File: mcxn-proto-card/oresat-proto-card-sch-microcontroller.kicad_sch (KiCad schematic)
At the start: 25 parts, among them J7 ORESAT-DEBUG-CONNECTOR-ALL, U1 TCAN330, U7 STM32F091C, X2 CRYSTAL-WITH-GND

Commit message: Removed and replaced eagle libraries for C, R, and Power symbols
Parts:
- C13, C14, C15, C18, C19, C20, C21: symbol oresat-proto-card-eagle-import:C-EU0603-C-NOSILK -> Device:C_Small_US
- D5: symbol oresat-proto-card-eagle-import:LED-GREEN0603 -> Device:D_Small_Filled
- JP11, JP8: symbol oresat-proto-card-eagle-import:PINHD-2X10 -> Connector_Generic:Conn_02x10_Odd_Even
- R47, R48, R49, R50, R51: symbol oresat-proto-card-eagle-import:R-US_0603-C-NOSILK -> oresat-passives:R-US
- TP25, TP26, TP27, TP28, TP29, TP30: value TEST-POINT-LARGE-SQUARE -> Test-Point; footprint oresat-proto-card:1X01 -> oresat-misc:TestPoint-0.75mm-th; symbol oresat-proto-card-eagle-import:TEST-POINT-LARGE-SQUARE -> oresat-misc:Test-Point-0.75mm-th; now left out of the parts list
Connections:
- net GND: now also D5.1 (K); no longer D5.C
- net at R48.1: now also D5.2 (A); no longer D5.A

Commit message: Eagle libraries removed and replaced, schematic and layout clean up
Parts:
- C13, C14, C15, C18, C19, C20, C21: symbol Device:C_Small_US -> Device:C_Small
- D5: footprint oresat-proto-card:LED-0603 -> LED_SMD:LED_0603_1608Metric; symbol Device:D_Small_Filled -> Device:LED_Small_Filled
- J7: footprint oresat-proto-card:TE_2-1734592-0 -> oresat-connectors:J-TE-2-1734592-0; symbol oresat-proto-card-eagle-import:ORESAT-DEBUG-CONNECTOR-ALL -> oresat-connectors:oresat-debug-all
- JP11, JP8: footprint oresat-proto-card:2X10 -> Connector_PinHeader_2.54mm:PinHeader_2x10_P2.54mm_Vertical
- U1: footprint oresat-proto-card:SOT23-8_TI-DCN -> oresat-ics:SOT23-8_TI-DCN; symbol oresat-proto-card-eagle-import:TCAN330 -> oresat-ics:TCAN330; Distributor (none) -> DigiKey; MPN TCAN330GDCNT -> TCAN330GDCN
- X2: footprint oresat-proto-card:CRYSTAL_2.5X2 -> Crystal:Crystal_SMD_2520-4Pin_2.5x2.0mm; symbol oresat-proto-card-eagle-import:CRYSTAL-WITH-GND -> Device:Crystal_GND2_Small
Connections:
- net GND: no longer X2.4 (SHIELD)
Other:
- note added: "NOT YELLOW!! (Also, on PCB there is a courtyard issue with new footprint, but I don't want to move it case it connects to backplane or something)"
- note added: "it is labeled: STM32F091C HOWEVER the MPN is labeled: STM32F042K6T Which one is it????"
- note added: "written on this page BUT applies to 2nd page as well. (except for that weird 10k thingy)"

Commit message: Eagle libraries replaced, scheatic and layout clean up cont.
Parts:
- removed U1: TCAN330, oresat-ics:SOT23-8_TI-DCN, symbol oresat-ics:TCAN330
- added U4: TCAN330, Package_TO_SOT_SMD:SOT-23-8, symbol Interface_CAN_LIN:TCAN330
- J7: footprint oresat-connectors:J-TE-2-1734592-0 -> oresat-proto-card:TE_2-1734592-0; symbol oresat-connectors:oresat-debug-all -> oresat-connectors:ORESAT-DEBUG-CONNECTOR-ALL
- R50, R51: now not fitted
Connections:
- net 3.3V: now also U4.3 (VCC)
- net CAN2_H: now also U4.7 (CANH)
- net CAN2_L: now also U4.6 (CANL)
- net CAN_RX: now also U4.4 (RXD)
- net CAN_SHDN: now also U4.5 (SHDN)
- net CAN_TX: now also U4.1 (TXD)
- net GND: now also U4.2 (GND)
- net PA9/CAN_SILENT: now also U4.8 (S)
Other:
- note removed: "Emergency M0 bootstrapping over OPD I2C Address: 0b0111110x"
- note removed: "NOT YELLOW!! (Also, on PCB there is a courtyard issue with new footprint, but I don't want to move it case it connects to backplane or something)"

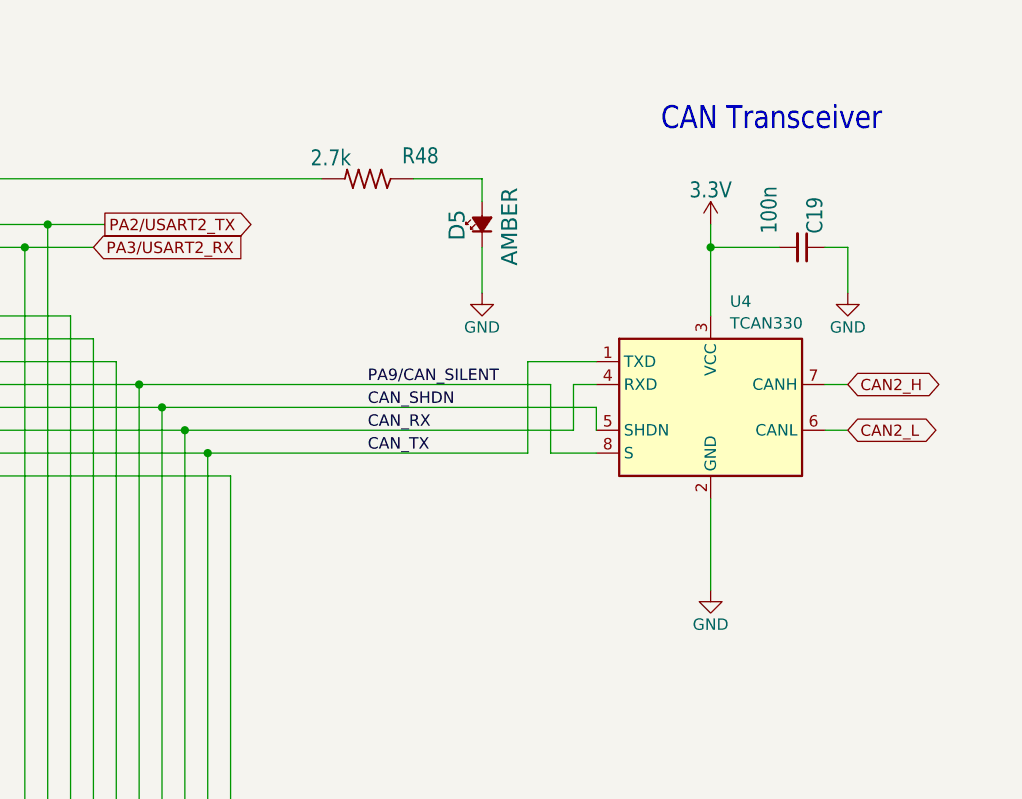
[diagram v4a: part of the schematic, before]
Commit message: Cleaned up layout and routing
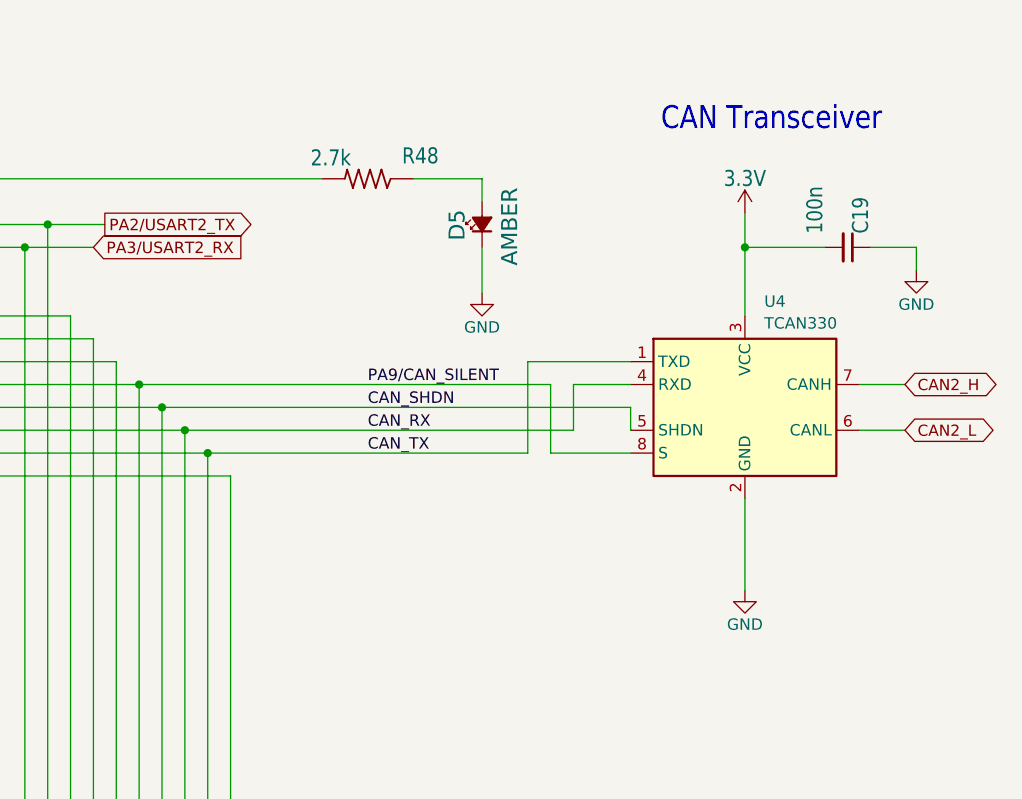
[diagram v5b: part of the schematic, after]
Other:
- moved on the sheet: C19, U4
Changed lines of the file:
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@@
 	)
 	(junction
-		(at 383.54 87.63)
-		(diameter 0)
-		(color 0 0 0 0)
-	)
-	(junction
 		(at 68.58 74.93)
 		(diameter 0)
@@
 	)
 	(junction
+		(at 387.35 87.63)
+		(diameter 0)
+		(color 0 0 0 0)
+	)
+	(junction
 		(at 220.98 21.59)
 		(diameter 0)
@@
 	(wire
 		(pts
-			(xy 383.54 87.63) (xy 391.16 87.63)
-		)
-		(stroke
-			(width 0.1524)
-			(type solid)
-		)
-	)
-	(wire
-		(pts
 			(xy 116.84 229.87) (xy 142.24 229.87)
 		)
@@
 	(wire
 		(pts
-			(xy 398.78 87.63) (xy 398.78 92.71)
+			(xy 406.4 87.63) (xy 406.4 90.17)
 		)
 		(stroke
@@
 	(wire
 		(pts
-			(xy 383.54 87.63) (xy 383.54 95.25)
+			(xy 387.35 87.63) (xy 387.35 95.25)
 		)
 		(stroke
@@
 	(wire
 		(pts
+			(xy 387.35 115.57) (xy 387.35 125.73)
+		)
+		(stroke
+			(width 0.1524)
+			(type solid)
+		)
+	)
+	(wire
+		(pts
 			(xy 43.18 57.15) (xy 33.02 57.15)
 		)
@@
 	(wire
 		(pts
-			(xy 322.58 105.41) (xy 370.84 105.41)
+			(xy 322.58 105.41) (xy 374.65 105.41)
 		)
 		(stroke
@@
 	(wire
 		(pts
-			(xy 396.24 87.63) (xy 398.78 87.63)
+			(xy 401.32 87.63) (xy 406.4 87.63)
 		)
 		(stroke
@@
 	(wire
 		(pts
-			(xy 383.54 87.63) (xy 383.54 85.09)
+			(xy 387.35 87.63) (xy 387.35 83.82)
 		)
 		(stroke
@@
 	(wire
 		(pts
-			(xy 365.76 110.49) (xy 370.84 110.49)
+			(xy 365.76 110.49) (xy 374.65 110.49)
 		)
 		(stroke
@@
 	(wire
 		(pts
-			(xy 383.54 115.57) (xy 383.54 125.73)
-		)
-		(stroke
-			(width 0.1524)
-			(type solid)
-		)
-	)
-	(wire
-		(pts
 			(xy 271.78 163.83) (xy 271.78 90.17)
 		)
@@
 	(wire
 		(pts
-			(xy 370.84 100.33) (xy 363.22 100.33)
+			(xy 374.65 100.33) (xy 363.22 100.33)
 		)
 		(stroke
@@
 	(wire
 		(pts
-			(xy 396.24 102.87) (xy 398.78 102.87)
+			(xy 400.05 102.87) (xy 405.13 102.87)
 		)
 		(stroke
@@
 	(wire
 		(pts
-			(xy 396.24 107.95) (xy 398.78 107.95)
+			(xy 400.05 107.95) (xy 405.13 107.95)
 		)
 		(stroke
@@
 	(wire
 		(pts
-			(xy 370.84 102.87) (xy 368.3 102.87)
+			(xy 374.65 102.87) (xy 368.3 102.87)
 		)
 		(stroke
@@
 	(wire
 		(pts
+			(xy 387.35 87.63) (xy 396.24 87.63)
+		)
+		(stroke
+			(width 0.1524)
+			(type solid)
+		)
+	)
+	(wire
+		(pts
 			(xy 246.38 82.55) (xy 279.4 82.55)
 		)
@@
 	(wire
 		(pts
-			(xy 370.84 105.41) (xy 370.84 107.95)
+			(xy 374.65 105.41) (xy 374.65 107.95)
 		)
 		(stroke
@@
 	(global_label "CAN2_L"
 		(shape bidirectional)
-		(at 398.78 107.95 0)
+		(at 405.13 107.95 0)
 		(fields_autoplaced yes)
 		(effects
@@
 		)
 		(property "Intersheetrefs" "${INTERSHEET_REFS}"
-			(at 409.5506 107.95 0)
+			(at 415.9006 107.95 0)
 			(effects
 				(font
@@
 	(global_label "CAN2_H"
 		(shape bidirectional)
-		(at 398.78 102.87 0)
+		(at 405.13 102.87 0)
 		(fields_autoplaced yes)
 		(effects
@@
 		)
 		(property "Intersheetrefs" "${INTERSHEET_REFS}"
-			(at 409.847 102.87 0)
+			(at 416.197 102.87 0)
 			(effects
 				(font
@@
 	(symbol
 		(lib_id "Device:C_Small")
-		(at 393.7 87.63 270)
+		(at 398.78 87.63 270)
 		(mirror x)
 		(unit 1)
@@
 		(dnp no)
 		(property "Reference" "C19"
-			(at 394.081 86.106 0)
+			(at 399.161 86.106 0)
 			(effects
 				(font
@@
 		)
 		(property "Value" "100n"
-			(at 389.001 86.106 0)
+			(at 394.081 86.106 0)
 			(effects
 				(font
@@
 		)
 		(property "Footprint" "oresat-passives:0603-C-NOSILK"
-			(at 393.7 87.63 0)
+			(at 398.78 87.63 0)
 			(effects
 				(font
@@
 		)
 		(property "Datasheet" "~"
-			(at 393.7 87.63 0)
+			(at 398.78 87.63 0)
 			(effects
 				(font
@@
 		)
 		(property "Description" "Unpolarized capacitor, small symbol"
-			(at 393.7 87.63 0)
+			(at 398.78 87.63 0)
 			(effects
 				(font
@@
 		)
 		(property "DIS" "Digi-Key"
-			(at 393.7 87.63 0)
+			(at 398.78 87.63 0)
 			(effects
 				(font
@@
 		)
 		(property "DPN" "1276-1001-1-ND"
-			(at 393.7 87.63 0)
+			(at 398.78 87.63 0)
 			(effects
 				(font
@@
 		)
 		(property "MFR" "Samsung"
-			(at 393.7 87.63 0)
+			(at 398.78 87.63 0)
 			(effects
 				(font
@@
 		)
 		(property "MPN" "CL05B104KO5NNNC"
-			(at 393.7 87.63 0)
+			(at 398.78 87.63 0)
 			(effects
 				(font
@@
 	(symbol
 		(lib_id "power:GND")
-		(at 383.54 125.73 0)
+		(at 387.35 125.73 0)
 		(mirror y)
 		(unit 1)
@@
 		(dnp no)
 		(property "Reference" "#GND057"
-			(at 383.54 125.73 0)
+			(at 387.35 125.73 0)
 			(effects
 				(font
@@
 		)
 		(property "Value" "GND"
-			(at 383.54 129.54 0)
+			(at 387.35 129.54 0)
 			(effects
 				(font
@@
 		)
 		(property "Footprint" ""
-			(at 383.54 125.73 0)
+			(at 387.35 125.73 0)
 			(effects
 				(font
@@
 		)
 		(property "Datasheet" ""
-			(at 383.54 125.73 0)
+			(at 387.35 125.73 0)
 			(effects
 				(font
@@
 		)
 		(property "Description" "Power symbol creates a global label with name \"GND\" , ground"
-			(at 383.54 125.73 0)
+			(at 387.35 125.73 0)
 			(effects
 				(font
@@
 	(symbol
 		(lib_id "power:+3.3V")
-		(at 383.54 85.09 0)
+		(at 387.35 83.82 0)
 		(mirror y)
 		(unit 1)
@@
 		(dnp no)
 		(property "Reference" "#SUPPLY09"
-			(at 383.54 85.09 0)
+			(at 387.35 83.82 0)
 			(effects
 				(font
@@
 		)
 		(property "Value" "3.3V"
-			(at 383.54 82.296 0)
+			(at 387.35 81.026 0)
 			(effects
 				(font
@@
 		)
 		(property "Footprint" ""
-			(at 383.54 85.09 0)
+			(at 387.35 83.82 0)
 			(effects
 				(font
@@
 		)
 		(property "Datasheet" ""
-			(at 383.54 85.09 0)
+			(at 387.35 83.82 0)
 			(effects
 				(font
@@
 		)
 		(property "Description" "Power symbol creates a global label with name \"+3.3V\""
-			(at 383.54 85.09 0)
+			(at 387.35 83.82 0)
 			(effects
 				(font
@@
 	(symbol
 		(lib_id "Interface_CAN_LIN:TCAN330")
-		(at 383.54 105.41 0)
+		(at 387.35 105.41 0)
 		(unit 1)
 		(exclude_from_sim no)
@@
 		(fields_autoplaced yes)
 		(property "Reference" "U4"
-			(at 385.6833 93.6455 0)
+			(at 389.4933 93.6455 0)
 			(effects
 				(font
@@
 		)
 		(property "Value" "TCAN330"
-			(at 385.6833 96.0698 0)
+			(at 389.4933 96.0698 0)
 			(effects
 				(font
@@
 		)
 		(property "Footprint" "Package_TO_SOT_SMD:SOT-23-8"
-			(at 383.54 118.11 0)
+			(at 387.35 118.11 0)
 			(effects
 				(font
@@
 		)
 		(property "Datasheet" "http://www.ti.com/lit/ds/symlink/tcan337.pdf"
-			(at 383.54 105.41 0)
+			(at 387.35 105.41 0)
 			(effects
 				(font
@@
 		)
 		(property "Description" "High-Speed CAN Transceiver, 1Mbps, 3.3V supply, silent mode, shutdown mode, SOT-23-8/SOIC-8"
-			(at 383.54 105.41 0)
+			(at 387.35 105.41 0)
 			(effects
 				(font
@@
 	(symbol
 		(lib_id "power:GND")
-		(at 398.78 92.71 0)
+		(at 406.4 90.17 0)
 		(mirror y)
 		(unit 1)
@@
 		(dnp no)
 		(property "Reference" "#GND056"
-			(at 398.78 92.71 0)
+			(at 406.4 90.17 0)
 			(effects
 				(font
@@
 		)
 		(property "Value" "GND"
-			(at 398.78 96.52 0)
+			(at 406.4 93.98 0)
 			(effects
 				(font
@@
 		)
 		(property "Footprint" ""
-			(at 398.78 92.71 0)
+			(at 406.4 90.17 0)
 			(effects
 				(font
@@
 		)
 		(property "Datasheet" ""
-			(at 398.78 92.71 0)
+			(at 406.4 90.17 0)
 			(effects
 				(font
@@
 		)
 		(property "Description" "Power symbol creates a global label with name \"GND\" , ground"
-			(at 398.78 92.71 0)
+			(at 406.4 90.17 0)
 			(effects
 				(font

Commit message: Fixed linked library footprints and routing
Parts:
- J7: footprint oresat-proto-card:TE_2-1734592-0 -> oresat-connectors:J-TE-2-1734592-0
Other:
- note added: "Look at datasheet pg 30. Different layout guideline for filtering and etc (for 3MHz to 3GHz)"
- note removed: "it is labeled: STM32F091C HOWEVER the MPN is labeled: STM32F042K6T Which one is it????"
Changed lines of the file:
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@@
 		)
 	)
-	(text "it is labeled: STM32F091C\nHOWEVER the MPN is labeled: STM32F042K6T\nWhich one is it????"
+	(text "Look at datasheet pg 30. Different layout guideline for filtering and etc (for 3MHz to 3GHz)"
 		(exclude_from_sim no)
-		(at 231.14 128.524 0)
+		(at 379.984 118.11 0)
 		(effects
 			(font
 				(size 1.27 1.27)
 			)
-			(justify left)
 		)
 	)
@@
 				)
 				(justify left bottom)
-				(hide yes)
 			)
 		)
@@
 			)
 		)
-		(property "Footprint" "oresat-proto-card:TE_2-1734592-0"
+		(property "Footprint" "oresat-connectors:J-TE-2-1734592-0"
 			(at 26.67 191.77 0)
 			(effects

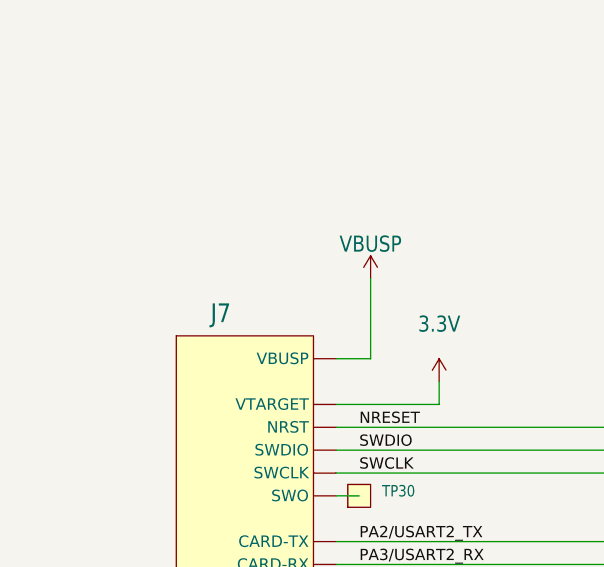
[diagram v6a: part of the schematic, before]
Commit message: Fixed schematic and routing for 2x11 connector
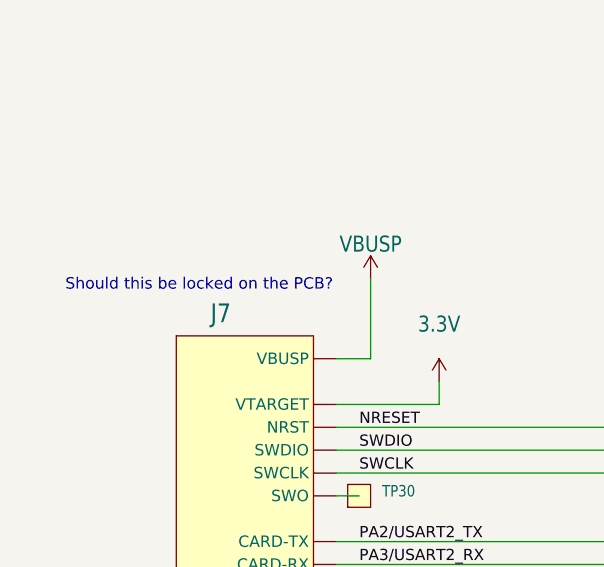
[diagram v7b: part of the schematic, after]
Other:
- note added: "Should this be locked on the PCB?"
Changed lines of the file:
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@@
+		)
+	)
+	(text "Should this be locked on the PCB?"
+		(exclude_from_sim no)
+		(at 22.86 155.702 0)
+		(effects
+			(font
+				(size 1.27 1.27)
+			)
 		)
 	)

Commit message: Fully routed MCXN947 proto card, still needs final polish.
Big cleanup of the proto card's OPD, bringing it up to modern standards. Also fixed the v2 backplane connector. Added the MCXN937 processor, and breakouts for the unused pins. Switched to the new debug connector, which will be fun. That's it!
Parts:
- removed C13, C14, C19, C20, C21: 100n, oresat-passives:0603-C-NOSILK, symbol Device:C_Small
- removed C15, C18: 20p, oresat-passives:0603-C-NOSILK, symbol Device:C_Small
- removed D5: AMBER, LED_SMD:LED_0603_1608Metric, symbol Device:LED_Small_Filled
- removed J7: ORESAT-DEBUG-CONNECTOR-ALL, oresat-connectors:J-TE-2-1734592-0, symbol oresat-connectors:ORESAT-DEBUG-CONNECTOR-ALL
- removed JP11, JP8: PINHD-2X10, Connector_PinHeader_2.54mm:PinHeader_2x10_P2.54mm_Vertical, symbol Connector_Generic:Conn_02x10_Odd_Even
- removed R47, R49: 10k, oresat-passives:0603-C-NOSILK, symbol oresat-passives:R-US
- removed R48: 2.7k, oresat-passives:0603-C-NOSILK, symbol oresat-passives:R-US
- removed R50, R51: 4.7k, oresat-passives:0603-C-NOSILK, symbol oresat-passives:R-US
- removed U4: TCAN330, Package_TO_SOT_SMD:SOT-23-8, symbol Interface_CAN_LIN:TCAN330
- removed U7: STM32F091C, oresat-proto-card:STM32F091C, symbol oresat-proto-card-eagle-import:STM32F091C
- removed X2: CRYSTAL-WITH-GND, Crystal:Crystal_SMD_2520-4Pin_2.5x2.0mm, symbol Device:Crystal_GND2_Small
- added C12, C24, C26, C28, C46, C48, C49, C50, C51, C52, C53, C7: 100n, oresat-passives:0603-C-NOSILK, symbol Device:C_Small
- added C25, C6: 4.7p, oresat-passives:0603-C-NOSILK, symbol Device:C_Small
- added C27, C30: 4.7u, oresat-passives:0603-C-NOSILK, symbol Device:C_Small
- added C29: 6.8u, oresat-passives:0603-C-NOSILK, symbol Device:C_Small
- added C31: 2.2u, oresat-passives:0603-C-NOSILK, symbol Device:C_Small
- added C47: 1u, oresat-passives:0603-C-NOSILK, symbol Device:C_Small
- added D4: AMBER, LED_SMD:LED_0603_1608Metric, symbol Device:LED_Small_Filled
- added FB1: 120 ohm, oresat-passives:0805-B-NOSILK, symbol Device:FerriteBead_Small
- added J9: SM14B-SHLS-TF, oresat-connectors:J-JST-SM14BSHLSTF, symbol oresat-connectors:ORESAT-DEBUG-CONNECTOR-3
- added L3: 1.5u, Inductor_SMD:L_0805_2012Metric, symbol Device:L_Small
- added R15: 10k, oresat-passives:0603-C-NOSILK, symbol Device:R_Small_US
- added R21: 1k, oresat-passives:0603-C-NOSILK, symbol Device:R_US
- added R23, R8: 4.7k, oresat-passives:0603-C-NOSILK, symbol Device:R_US
- added R9: 10k, oresat-passives:0603-C-NOSILK, symbol Device:R_US
- added TP10, TP11, TP12, TP13, TP14, TP16, TP17, TP18, TP19, TP20, TP22, TP3, TP32, TP33, TP41, TP42, TP43, TP44, TP45, TP46, TP47, TP48, TP49, TP5, TP50, TP51, TP52, TP53, TP54, TP55, TP56, TP57, TP58, TP59, TP6, TP60, TP61, TP62, TP63, TP64, TP65, TP66, TP67, TP68, TP69, TP7, TP70, TP71, TP72, TP73, TP74, TP75, TP76, TP77, TP78, TP79, TP8, TP80, TP81, TP82, TP83, TP84, TP85, TP86, TP9: Test-Point, oresat-misc:TestPoint-0.75mm-th, symbol oresat-misc:Test-Point-0.75mm-th
- added U1: MCXN947VKLT, oresat-ics:MCXN947KVLT-QFP50P1600X1600X160-101N, symbol oresat-ics:MCXN947VKLT
- added U8: TCAN330, Package_TO_SOT_SMD:SOT-23-8, symbol Interface_CAN_LIN:TCAN330
- added Y2: 24 MHz, Crystal:Crystal_SMD_2016-4Pin_2.0x1.6mm, symbol Device:Crystal_GND24_Small
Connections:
- net CAN2_H: now also U8.7 (CANH)
- net CAN2_L: now also U8.6 (CANL)
- net GND: now also C12.2, C24.2, C25.2, C26.2, C27.2, C28.2, C29.2, C30.2, C31.2, C46.2, C47.2, C48.2, C49.2, C50.2, C51.2, C52.2, C53.2, C6.2, C7.2, D4.1 (K), J9.14 (GND), J9.15 (PAD), J9.16 (PAD), J9.5 (GND), U1.101 (EP), U1.32 (VREFL), U1.33 (VSS_P4), U1.52 (VSS_DCDC), U8.2 (GND), Y2.2, Y2.4
- net SWCLK: now also J9.12 (SWCLK), U1.77 (P0_1)
- net SWDIO: now also J9.11 (SWDIO), U1.76 (P0_0)
- net VBUSP: now also J9.1 (VBUSP), J9.2 (VBUSP)
- net P4_2: now reaches TP28.1
- net P4_2: now also U1.24 (P4_2)
- net P4_0: now reaches TP30.1
- net P4_0: now also U1.22 (P4_0/ANA_0)
- net P4_4: now reaches TP26.1
- net P4_4: now also U1.26 (P4_4/ANA_4)
- net P4_3: now reaches TP27.1
- net P4_3: now also U1.25 (P4_3)
- net P4_1: now reaches TP29.1
- net P4_1: now also U1.23 (P4_1/ANA_1)
- net BOOT0 renamed P4_5
- net P4_5: now also U1.27 (P4_5/ANA_5)
- new net: C6.1, U1.11 (P1_31), Y2.1
- new net: U1.3 (P1_10), U8.1 (TXD)
- new net: U1.4 (P1_11), U8.4 (RXD)
- new net: C25.1, U1.10 (P1_30), Y2.3
- new net: D4.2 (A), R21.2
- new net: R21.1, U1.6 (P1_13)
- new net: J9.8 (DEBUG-0), TP6.1
- new net: L3.2, U1.53 (DCDC_LX)
- new net +3.3V: C24.1, C28.1, C30.1, C46.1, C48.1, C49.1, C50.1, C51.1, C52.1, C53.1, C7.1, FB1.1, J9.9 (VTARGET), R15.2, R23.2, R8.2, R9.2, U1.13 (VDD_LDO_CORE/VDD/VDD_P2), U1.34 (VDD_P4), U1.44 (VDD_USB), U1.47 (VDD_BAT), U1.54 (VDD_DCDC/VDD_LDO_SYS), U1.59 (VDD_P3), U1.66 (VDD_P3), U1.73 (VDD_P3), U1.83 (VDD), U1.96 (VDD), U8.3 (VCC)
- new net ISP-UART_RXD: J9.7 (CARD-RX), TP3.1, U1.1 (P1_8)
- new net ISP-UART_TXD: J9.6 (CARD-TX), TP13.1, U1.2 (P1_9)
- new net P0_18: TP78.1, U1.86 (P0_18)
- new net P0_19: TP79.1, U1.87 (P0_19)
- new net P0_20: TP80.1, U1.88 (P0_20)
- new net P0_21: TP81.1, U1.89 (P0_21)
- new net P0_22: TP82.1, U1.90 (P0_22)
- new net P0_23: TP83.1, U1.91 (P0_23)
- new net P0_4: TP85.1, U1.80 (P0_4)
- new net P0_5: TP86.1, U1.81 (P0_5)
- new net P1_0: TP68.1, U1.92 (P1_0)
- new net P1_1: TP69.1, U1.93 (P1_1)
- new net P1_12: TP5.1, U1.5 (P1_12)
- new net P1_14: TP7.1, U1.7 (P1_14)
- new net P1_15: TP8.1, U1.8 (P1_15)
- new net P1_2: TP70.1, U1.94 (P1_2)
- new net P1_3: TP71.1, U1.95 (P1_3)
- new net P1_4: TP72.1, U1.97 (P1_4)
- new net P1_5: TP73.1, U1.98 (P1_5)
- new net P1_6: TP74.1, U1.99 (P1_6)
- new net P1_7: TP75.1, U1.100 (P1_7)
- new net P2_0: TP9.1, U1.14 (P2_0)
- new net P2_1: TP10.1, U1.15 (P2_1)
- new net P2_2: TP11.1, U1.16 (P2_2)
- new net P2_3: TP12.1, U1.17 (P2_3)
- new net P2_4: TP14.1, U1.18 (P2_4)
- new net P2_5: TP17.1, U1.19 (P2_5)
- new net P2_6: TP18.1, U1.20 (P2_6)
- new net P2_7: TP19.1, U1.21 (P2_7)
- new net P3_0: TP53.1, U1.75 (P3_0)
- new net P3_1: TP52.1, U1.74 (P3_1)
- new net P3_10: TP47.1, U1.68 (P3_10)
- new net P3_11: TP61.1, U1.67 (P3_11)
- new net P3_12: TP60.1, U1.65 (P3_12)
- new net P3_13: TP59.1, U1.64 (P3_13)
- new net P3_14: TP58.1, U1.63 (P3_14)
- new net P3_15: TP57.1, U1.62 (P3_15)
- new net P3_16: TP56.1, U1.61 (P3_16)
- new net P3_17: TP55.1, U1.60 (P3_17)
- new net P3_20: TP62.1, U1.57 (P3_20)
- new net P3_21: TP63.1, U1.56 (P3_21)
- new net P3_6: TP51.1, U1.72 (P3_6)
- new net P3_7: TP50.1, U1.71 (P3_7)
- new net P3_8: TP49.1, U1.70 (P3_8)
- new net P3_9: TP48.1, U1.69 (P3_9)
- new net P4_12: TP46.1, U1.35 (P4_12)
- new net P4_13: TP45.1, U1.36 (P4_13/ANA_14)
- new net P4_15: TP44.1, U1.37 (P4_15)
- new net P4_16: TP43.1, U1.38 (P4_16)
- new net P4_17: TP42.1, U1.39 (P4_17/ANA_18)
- new net P4_19: TP41.1, U1.40 (P4_19)
- new net P4_20: TP33.1, U1.41 (P4_20)
- new net P4_21: TP32.1, U1.42 (P4_21/ANA_22)
- new net P4_23: TP54.1, U1.43 (P4_23)
- new net P4_6: TP22.1, U1.28 (P4_6/ANA_6)
- new net P4_7: TP20.1, U1.29 (P4_7/ANA_7)
- new net P5_0: TP64.1, U1.48 (P5_0)
- new net P5_1: TP65.1, U1.49 (P5_1)
- new net P5_2: TP66.1, U1.50 (P5_2)
- new net P5_3: TP67.1, U1.51 (P5_3)
- new net RESET: C12.1, J9.10 (NRST), R15.1, TP16.1, U1.9 (RESET_B)
- new net SCL: R8.1, TP77.1, U1.85 (P0_17)
- new net SDA: R23.1, TP76.1, U1.84 (P0_16)
- new net SWO: J9.13 (SWO), U1.78 (P0_2)
- new net TDI : TP84.1, U1.79 (P0_3)
- new net VDD_ANA: C47.1, FB1.2, U1.30 (VDD_ANA), U1.31 (VREFH)
- new net VDD_CORE: C26.1, C27.1, C29.1, L3.1, U1.12 (VDD_CORE), U1.58 (VDD_CORE)
- new net VDD_SYS: C31.1, U1.55 (VDD_SYS)
- new net ~{BOOT}: R9.1, U1.82 (P0_6)
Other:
- note added: "24 MHz allows LPTMRs to work"
- note added: "All caps are ceramic 10% X5R >= 16V Vwv and AEQ unless marked"
- note added: "All resistors 0603 +/- 1% and AEQ unless marked"
- note added: "Connect to CAN2 because the proto card isn't part of critical systems."
- note added: "Note: Disable LDO_CORE in software for more power savings"
- note added: "OreSat Debug Connector"
- note added: "P0/P1"
- note added: "RX-TX cross on DEBUG board"
- note added: "VDD_BAT"
- note removed: "All caps are ceramic 10% X5R >= 16V V unless marked"
- note removed: "All resistors 0603 +/- 1% unless marked"
- note removed: "GPIO Breakouts"
- note removed: "Look at datasheet pg 30. Different layout guideline for filtering and etc (for 3MHz to 3GHz)"
- note removed: "NRST pull-up built in"
- note removed: "Power/Current draw from OPD. Signal is analog voltage 0-1.2V"
- note removed: "Rx-Tx switch happens on programming board"
- note removed: "Should this be locked on the PCB?"
- note removed: "VBAT not bypassed becase not enough room instead tied into nearest bypass cap"
- note removed: "written on this page BUT applies to 2nd page as well. (except for that weird 10k thingy)"
- title: OreSat M0 Proto Card: Microcontroller -> OreSat MCXN Proto Card
